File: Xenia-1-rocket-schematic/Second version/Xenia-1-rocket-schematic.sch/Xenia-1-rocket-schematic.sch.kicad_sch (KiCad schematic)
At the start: 4 parts

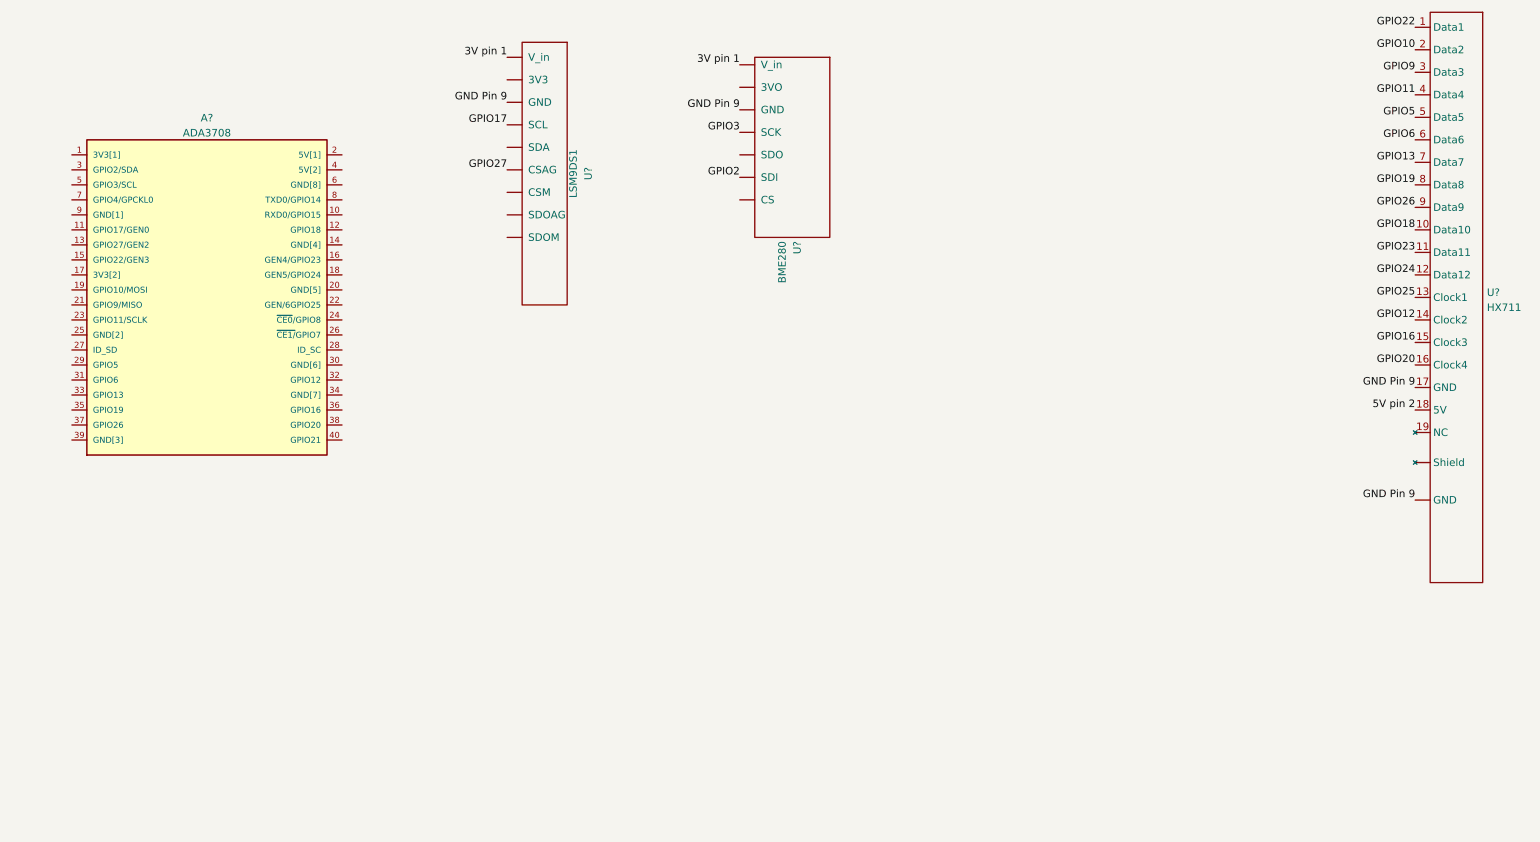
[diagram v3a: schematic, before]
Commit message: Changing the power pins to wires
All the ground pins have been connected to the ground pin 9, and all the power pins are now connected to wires.
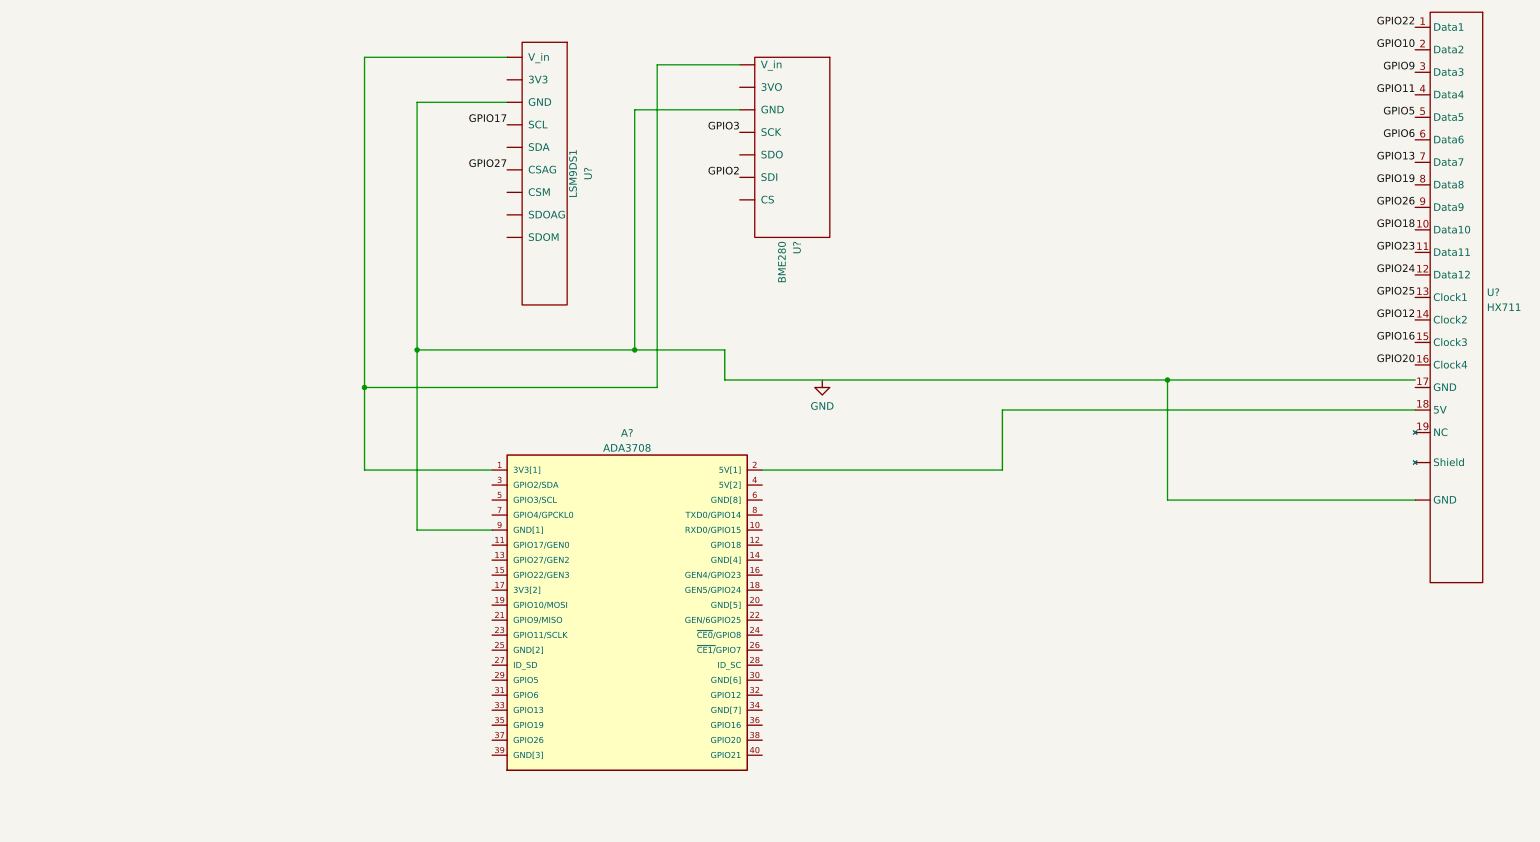
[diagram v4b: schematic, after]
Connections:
- net 5V pin 2 is gone; now on an unnamed net: U?.18 (5V)
- net at A?.1 (3V3[1]): now also U?.~ (V_in), U?.~ (V_in)
- net at A?.9 (GND[1]): now also U?. (Shield), U?.~ (V_in), U?.~ (V_in)
- removed net 3V pin 1: U?.~ (V_in), U?.~ (V_in)
- removed net GND Pin 9: U?. (Shield), U?.17 (GND), U?.~ (V_in), U?.~ (V_in)
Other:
- moved on the sheet: A?
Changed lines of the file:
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@@
 (kicad_sch (version 20211123) (generator eeschema)
   (paper "A4")
+  (junction (at 119.38 71.12) (diameter 0) (color 0 0 0 0)
+  )
+  (junction (at 209.55 76.2) (diameter 0) (color 0 0 0 0)
+  )
+  (junction (at 73.66 77.47) (diameter 0) (color 0 0 0 0)
+  )
+  (junction (at 82.55 71.12) (diameter 0) (color 0 0 0 0)
+  )
+  (wire (pts (xy 119.38 30.48) (xy 119.38 71.12))
+    (stroke (width 0) (type default) (color 0 0 0 0))
+  )
+  (wire (pts (xy 181.61 81.28) (xy 181.61 91.44))
+    (stroke (width 0) (type default) (color 0 0 0 0))
+  )
+  (wire (pts (xy 97.79 21.59) (xy 73.66 21.59))
+    (stroke (width 0) (type default) (color 0 0 0 0))
+  )
+  (wire (pts (xy 134.62 76.2) (xy 134.62 71.12))
+    (stroke (width 0) (type default) (color 0 0 0 0))
+  )
+  (wire (pts (xy 82.55 29.21) (xy 82.55 71.12))
+    (stroke (width 0) (type default) (color 0 0 0 0))
+  )
+  (wire (pts (xy 73.66 77.47) (xy 73.66 91.44))
+    (stroke (width 0) (type default) (color 0 0 0 0))
+  )
+  (wire (pts (xy 82.55 71.12) (xy 119.38 71.12))
+    (stroke (width 0) (type default) (color 0 0 0 0))
+  )
+  (wire (pts (xy 251.46 81.28) (xy 181.61 81.28))
+    (stroke (width 0) (type default) (color 0 0 0 0))
+  )
+  (wire (pts (xy 82.55 71.12) (xy 82.55 101.6))
+    (stroke (width 0) (type default) (color 0 0 0 0))
+  )
+  (wire (pts (xy 251.46 76.2) (xy 209.55 76.2))
+    (stroke (width 0) (type default) (color 0 0 0 0))
+  )
+  (wire (pts (xy 137.16 30.48) (xy 119.38 30.48))
+    (stroke (width 0) (type default) (color 0 0 0 0))
+  )
+  (wire (pts (xy 209.55 96.52) (xy 209.55 76.2))
+    (stroke (width 0) (type default) (color 0 0 0 0))
+  )
+  (wire (pts (xy 137.16 22.86) (xy 123.19 22.86))
+    (stroke (width 0) (type default) (color 0 0 0 0))
+  )
+  (wire (pts (xy 251.46 96.52) (xy 209.55 96.52))
+    (stroke (width 0) (type default) (color 0 0 0 0))
+  )
+  (wire (pts (xy 123.19 77.47) (xy 73.66 77.47))
+    (stroke (width 0) (type default) (color 0 0 0 0))
+  )
+  (wire (pts (xy 123.19 22.86) (xy 123.19 77.47))
+    (stroke (width 0) (type default) (color 0 0 0 0))
+  )
+  (wire (pts (xy 97.79 29.21) (xy 82.55 29.21))
+    (stroke (width 0) (type default) (color 0 0 0 0))
+  )
+  (wire (pts (xy 73.66 21.59) (xy 73.66 77.47))
+    (stroke (width 0) (type default) (color 0 0 0 0))
+  )
+  (wire (pts (xy 134.62 71.12) (xy 119.38 71.12))
+    (stroke (width 0) (type default) (color 0 0 0 0))
+  )
+  (wire (pts (xy 209.55 76.2) (xy 134.62 76.2))
+    (stroke (width 0) (type default) (color 0 0 0 0))
+  )
+  (wire (pts (xy 82.55 101.6) (xy 95.25 101.6))
+    (stroke (width 0) (type default) (color 0 0 0 0))
+  )
+  (wire (pts (xy 181.61 91.44) (xy 140.97 91.44))
+    (stroke (width 0) (type default) (color 0 0 0 0))
+  )
+  (wire (pts (xy 73.66 91.44) (xy 95.25 91.44))
+    (stroke (width 0) (type default) (color 0 0 0 0))
+  )
   (label "GPIO13" (at 251.46 39.37 180)
     (effects (font (size 1.27 1.27)) (justify right bottom))
@@
     (effects (font (size 1.27 1.27)) (justify right bottom))
   )
-  (label "GND Pin 9" (at 137.16 30.48 180)
-    (effects (font (size 1.27 1.27)) (justify right bottom))
-  )
   (label "GPIO20" (at 251.46 73.66 180)
     (effects (font (size 1.27 1.27)) (justify right bottom))
@@
     (effects (font (size 1.27 1.27)) (justify right bottom))
   )
-  (label "3V pin 1" (at 97.79 21.59 180)
-    (effects (font (size 1.27 1.27)) (justify right bottom))
-  )
   (label "GPIO16" (at 251.46 69.85 180)
     (effects (font (size 1.27 1.27)) (justify right bottom))
@@
     (effects (font (size 1.27 1.27)) (justify right bottom))
   )
-  (label "GND Pin 9" (at 251.46 96.52 180)
-    (effects (font (size 1.27 1.27)) (justify right bottom))
-  )
   (label "GPIO17" (at 97.79 33.02 180)
     (effects (font (size 1.27 1.27)) (justify right bottom))
@@
     (effects (font (size 1.27 1.27)) (justify right bottom))
   )
-  (label "5V pin 2" (at 251.46 81.28 180)
-    (effects (font (size 1.27 1.27)) (justify right bottom))
-  )
-  (label "GND Pin 9" (at 97.79 29.21 180)
-    (effects (font (size 1.27 1.27)) (justify right bottom))
-  )
-  (label "GND Pin 9" (at 251.46 77.47 180)
-    (effects (font (size 1.27 1.27)) (justify right bottom))
-  )
   (label "GPIO27" (at 97.79 40.64 180)
     (effects (font (size 1.27 1.27)) (justify right bottom))
@@
     (effects (font (size 1.27 1.27)) (justify right bottom))
   )
-  (label "3V pin 1" (at 137.16 22.86 180)
-    (effects (font (size 1.27 1.27)) (justify right bottom))
-  )
-  (symbol (lib_id "ADA3708:ADA3708") (at 46.99 60.96 0) (unit 1)
-    (in_bom yes) (on_board yes) (fields_autoplaced)
-    (property "Reference" "A?" (id 0) (at 46.99 31.8602 0))
-    (property "Value" "ADA3708" (id 1) (at 46.99 34.3971 0))
-    (property "Footprint" "ADA3708_RPI-ZERO" (id 2) (at 46.99 60.96 0)
-      (effects (font (size 1.27 1.27)) (justify left bottom) hide)
-    )
-    (property "Datasheet" "" (id 3) (at 46.99 60.96 0)
-      (effects (font (size 1.27 1.27)) (justify left bottom) hide)
-    )
-    (property "MANUFACTURER" "Raspberry" (id 4) (at 46.99 60.96 0)
-      (effects (font (size 1.27 1.27)) (justify left bottom) hide)
-    )
-    (property "STANDARD" "MAnufactutrer Recommendations" (id 5) (at 46.99 60.96 0)
+  (symbol (lib_id "power:GND") (at 151.13 76.2 0) (unit 1)
+    (in_bom yes) (on_board yes) (fields_autoplaced)
+    (property "Reference" "#PWR?" (id 0) (at 151.13 82.55 0)
+      (effects (font (size 1.27 1.27)) hide)
+    )
+    (property "Value" "GND" (id 1) (at 151.13 80.6434 0))
+    (property "Footprint" "" (id 2) (at 151.13 76.2 0)
+      (effects (font (size 1.27 1.27)) hide)
+    )
+    (property "Datasheet" "" (id 3) (at 151.13 76.2 0)
+      (effects (font (size 1.27 1.27)) hide)
+    )
+    (pin "1")
+  )
+  (symbol (lib_id "ADA3708:ADA3708") (at 118.11 114.3 0) (unit 1)
+    (in_bom yes) (on_board yes) (fields_autoplaced)
+    (property "Reference" "A?" (id 0) (at 118.11 85.2002 0))
+    (property "Value" "ADA3708" (id 1) (at 118.11 87.7371 0))
+    (property "Footprint" "ADA3708_RPI-ZERO" (id 2) (at 118.11 114.3 0)
+      (effects (font (size 1.27 1.27)) (justify left bottom) hide)
+    )
+    (property "Datasheet" "" (id 3) (at 118.11 114.3 0)
+      (effects (font (size 1.27 1.27)) (justify left bottom) hide)
+    )
+    (property "MANUFACTURER" "Raspberry" (id 4) (at 118.11 114.3 0)
+      (effects (font (size 1.27 1.27)) (justify left bottom) hide)
+    )
+    (property "STANDARD" "MAnufactutrer Recommendations" (id 5) (at 118.11 114.3 0)
       (effects (font (size 1.27 1.27)) (justify left bottom) hide)
     )
@@
   )
   (symbol_instances
+    (path "/458cdc62-e3c9-4c6b-a506-564e5e44cc1c"
+      (reference "#PWR?") (unit 1) (value "GND") (footprint "")
+    )
     (path "/5c8b9a82-a605-41d3-a522-45a95276ab73"
       (reference "A?") (unit 1) (value "ADA3708") (footprint "ADA3708_RPI-ZERO")

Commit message: Added more components
Analog to digital converter added.
Black box added and pushed to diagram.
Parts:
- added U?: Black_Box, symbol Rocketry_project:Black_Box
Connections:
- net GPIO12: now also U?.15 (Clock3); no longer U?.14 (Clock2)
- net GPIO16: now also U?.16 (Clock4); no longer U?.15 (Clock3)
- net GPIO20: now also U?. (PCM_DOUT); no longer U?.16 (Clock4)
- net GPIO23: now also U?.12 (Data12); no longer U?.11 (Data11)
- net GPIO24: now also U?.13 (Clock1); no longer U?.12 (Data12)
- net GPIO25: now also U?.14 (Clock2); no longer U?.13 (Clock1)
- net GPIO18 renamed GPIO14
- new net: A?.1 (3V3[1]), U?.~ (V_in), U?.~ (V_in)
- new net: A?.9 (GND[1]), U?. (Shield), U?.~ (V_in), U?.~ (V_in)
- new net GPIO15: U?.11 (Data11)
- new net GPIO21: U?. (PCM_DOUT)
- now unconnected: U?. (Shield)
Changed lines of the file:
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@@
     (effects (font (size 1.27 1.27)) (justify right bottom))
   )
-  (label "GPIO12" (at 251.46 66.04 180)
+  (label "GPIO25" (at 251.46 66.04 180)
     (effects (font (size 1.27 1.27)) (justify right bottom))
   )
@@
     (effects (font (size 1.27 1.27)) (justify right bottom))
   )
-  (label "GPIO20" (at 251.46 73.66 180)
+  (label "GPIO21" (at 207.01 129.54 180)
+    (effects (font (size 1.27 1.27)) (justify right bottom))
+  )
+  (label "GPIO16" (at 251.46 73.66 180)
+    (effects (font (size 1.27 1.27)) (justify right bottom))
+  )
+  (label "GPIO20" (at 207.01 118.11 180)
     (effects (font (size 1.27 1.27)) (justify right bottom))
   )
@@
     (effects (font (size 1.27 1.27)) (justify right bottom))
   )
-  (label "GPIO16" (at 251.46 69.85 180)
-    (effects (font (size 1.27 1.27)) (justify right bottom))
-  )
-  (label "GPIO24" (at 251.46 58.42 180)
-    (effects (font (size 1.27 1.27)) (justify right bottom))
-  )
-  (label "GPIO25" (at 251.46 62.23 180)
-    (effects (font (size 1.27 1.27)) (justify right bottom))
-  )
-  (label "GPIO23" (at 251.46 54.61 180)
+  (label "GPIO12" (at 251.46 69.85 180)
+    (effects (font (size 1.27 1.27)) (justify right bottom))
+  )
+  (label "GPIO23" (at 251.46 58.42 180)
+    (effects (font (size 1.27 1.27)) (justify right bottom))
+  )
+  (label "GPIO24" (at 251.46 62.23 180)
+    (effects (font (size 1.27 1.27)) (justify right bottom))
+  )
+  (label "GPIO15" (at 251.46 54.61 180)
     (effects (font (size 1.27 1.27)) (justify right bottom))
   )
@@
     (effects (font (size 1.27 1.27)) (justify right bottom))
   )
-  (label "GPIO18" (at 251.46 50.8 180)
+  (label "GPIO14" (at 251.46 50.8 180)
     (effects (font (size 1.27 1.27)) (justify right bottom))
   )
@@
     (pin "9")
   )
+  (symbol (lib_id "Rocketry_project:Black_Box") (at 217.17 121.92 270) (unit 1)
+    (in_bom yes) (on_board yes) (fields_autoplaced)
+    (property "Reference" "U?" (id 0) (at 221.6912 123.6253 90)
+      (effects (font (size 1.27 1.27)) (justify left))
+    )
+    (property "Value" "Black_Box" (id 1) (at 221.6912 126.1622 90)
+      (effects (font (size 1.27 1.27)) (justify left))
+    )
+    (property "Footprint" "" (id 2) (at 217.17 121.92 0)
+      (effects (font (size 1.27 1.27)) hide)
+    )
+    (property "Datasheet" "" (id 3) (at 217.17 121.92 0)
+      (effects (font (size 1.27 1.27)) hide)
+    )
+    (pin "")
+    (pin "")
+  )
   (symbol (lib_id "Rocketry_project:BME280") (at 147.32 30.48 270) (unit 1)
     (in_bom yes) (on_board yes) (fields_autoplaced)
@@
       (reference "U?") (unit 1) (value "HX711") (footprint "")
     )
+    (path "/aa41ea04-69be-4e8f-824e-5173ea28f17d"
+      (reference "U?") (unit 1) (value "Black_Box") (footprint "")
+    )
     (path "/e5902a33-9c06-4340-a33e-d75bd8ccd20e"
